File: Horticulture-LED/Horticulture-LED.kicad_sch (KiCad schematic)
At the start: 61 parts, among them J3 Conn_01x04_Male, J4 Conn_01x04_Male, U1 TLE4309, U2 TLE4309, U3 TLE4309, U4 TLE4309, U5 PCA9633DP2, U6 MCP1703A-1502_SOT223

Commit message: Updated component reference
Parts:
- renumbered 3.3v_i2c1 to 3_3v_i2c1, 3.3v_i2c2 to 3_3v_i2c2, 3.3v_i2c3 to 3_3v_i2c3, 3.3v_i2c4 to 3_3v_i2c4
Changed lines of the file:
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@@
 		(on_board yes)
 		(dnp no)
-		(property "Reference" "3.3v_i2c1"
+		(property "Reference" "3_3v_i2c1"
 			(at 347.2688 199.8472 0)
 			(effects
@@
 			(project ""
 				(path "/922058ca-d09a-45fd-8394-05f3e2c1e03a"
-					(reference "3.3v_i2c1")
+					(reference "3_3v_i2c1")
 					(unit 1)
 				)
@@
 		(on_board yes)
 		(dnp no)
-		(property "Reference" "3.3v_i2c2"
+		(property "Reference" "3_3v_i2c2"
 			(at 347.2688 213.8172 0)
 			(effects
@@
 			(project ""
 				(path "/922058ca-d09a-45fd-8394-05f3e2c1e03a"
-					(reference "3.3v_i2c2")
+					(reference "3_3v_i2c2")
 					(unit 1)
 				)
@@
 		(on_board yes)
 		(dnp no)
-		(property "Reference" "3.3v_i2c3"
+		(property "Reference" "3_3v_i2c3"
 			(at 347.2688 226.5172 0)
 			(effects
@@
 			(project ""
 				(path "/922058ca-d09a-45fd-8394-05f3e2c1e03a"
-					(reference "3.3v_i2c3")
+					(reference "3_3v_i2c3")
 					(unit 1)
 				)
@@
 		(on_board yes)
 		(dnp no)
-		(property "Reference" "3.3v_i2c4"
+		(property "Reference" "3_3v_i2c4"
 			(at 347.2688 239.2172 0)
 			(effects
@@
 			(project ""
 				(path "/922058ca-d09a-45fd-8394-05f3e2c1e03a"
-					(reference "3.3v_i2c4")
-					(unit 1)
-				)
+					(reference "3_3v_i2c4")
+					(unit 1)
+				)

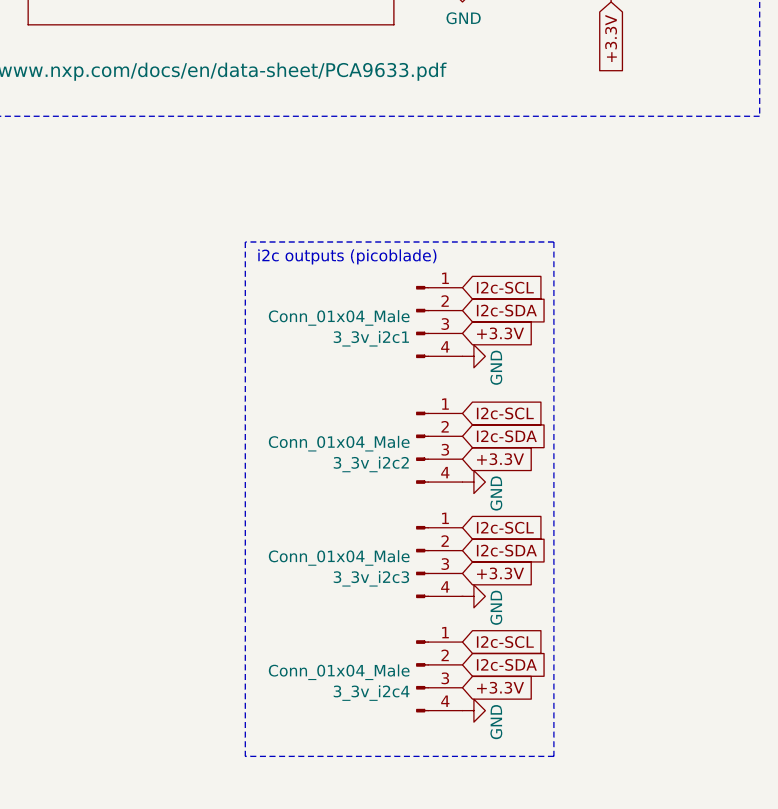
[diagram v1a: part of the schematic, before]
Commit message: Fixed 3.3V i2c references
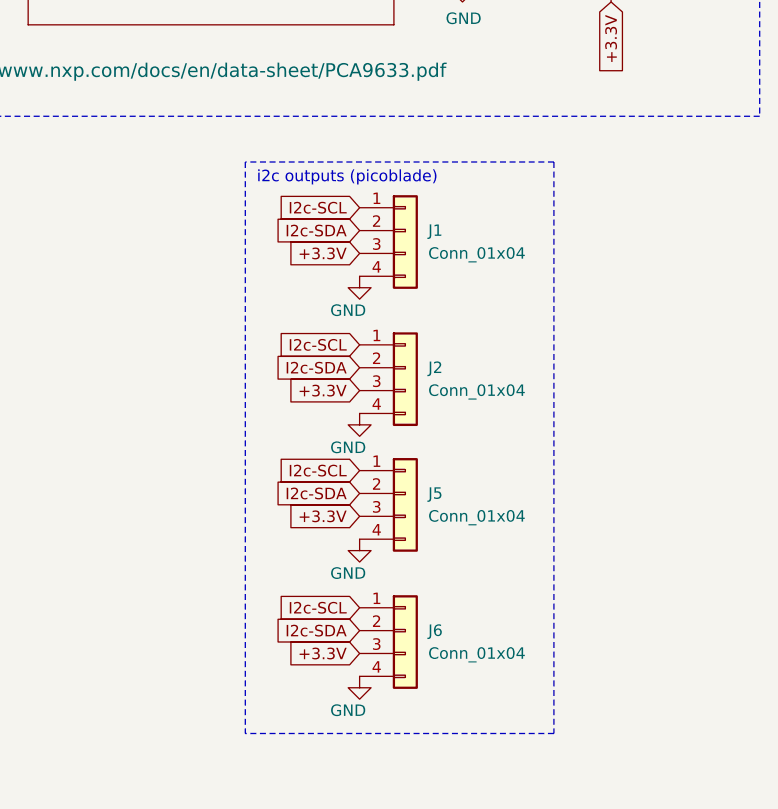
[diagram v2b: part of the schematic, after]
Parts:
- removed 3_3v_i2c1, 3_3v_i2c2, 3_3v_i2c3, 3_3v_i2c4: Conn_01x04_Male, Connector_Molex:Molex_PicoBlade_53398-0471_1x04-1MP_P1.25mm_Vertical, symbol Connector:Conn_01x04_Male
- added J1, J2, J5, J6: Conn_01x04, Connector_Molex:Molex_PicoBlade_53398-0471_1x04-1MP_P1.25mm_Vertical, symbol Connector_Generic:Conn_01x04
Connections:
- net +3.3V: now also J1.3 (Pin_3), J2.3 (Pin_3), J5.3 (Pin_3), J6.3 (Pin_3)
- net GND: now also J1.4 (Pin_4), J2.4 (Pin_4), J5.4 (Pin_4), J6.4 (Pin_4)
- net I2c-SCL: now also J1.1 (Pin_1), J2.1 (Pin_1), J5.1 (Pin_1), J6.1 (Pin_1)
- net I2c-SDA: now also J1.2 (Pin_2), J2.2 (Pin_2), J5.2 (Pin_2), J6.2 (Pin_2)
